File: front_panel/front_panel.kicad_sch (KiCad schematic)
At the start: 48 parts, among them J1 Conn_01x03_Socket, J10 Conn_01x02_Socket, J11 Conn_01x02_Socket, J12 Conn_01x02_Socket, J13 Conn_01x02_Socket, J14 Conn_01x02_Socket, J15 Conn_01x02_Socket, J16 Conn_01x02_Socket, J17 Conn_01x02_Socket, J18 Conn_01x02_Socket, J2 Conn_01x02_Socket, J20 Conn_01x02_Socket, J3 Conn_01x02_Socket, J4 Conn_01x04_Socket, J5 Conn_01x02_Socket, J5 Conn_01x03_Pin, J6 Conn_01x05_Pin, J7 Conn_01x02_Socket, J7 Conn_01x03_Pin, J8 Conn_01x02_Socket, J9 Conn_01x02_Socket, Q1 DMN3023L, Q2 DMN3023L, SW1 RotaryEncoder_Switch, SW2 SW_MEC_5G, SW3 SW_MEC_5G, U10 MCP9700x-ETT, U11 MCP33141D-05, U2 LM4040DBZ-4.1, U3 NCS21804, U4 CD74HC4067M, U5 DAC60501, U6 MIC5504-1.8YM5, U7 BP, U8 CD74HC4067M, U9 MCP9700x-ETT

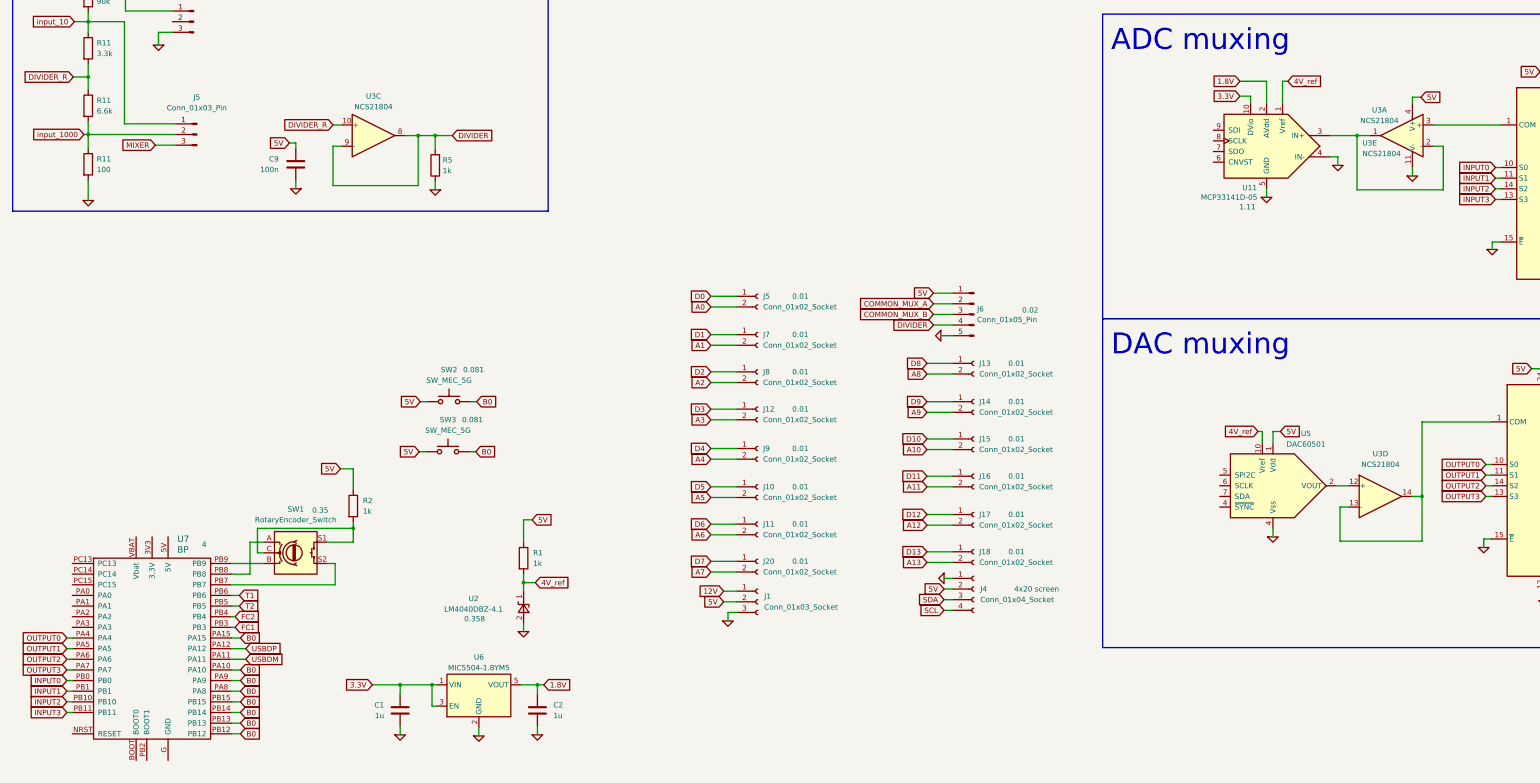
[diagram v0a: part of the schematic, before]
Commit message: Konačno PCB za BJT modul je počeo.
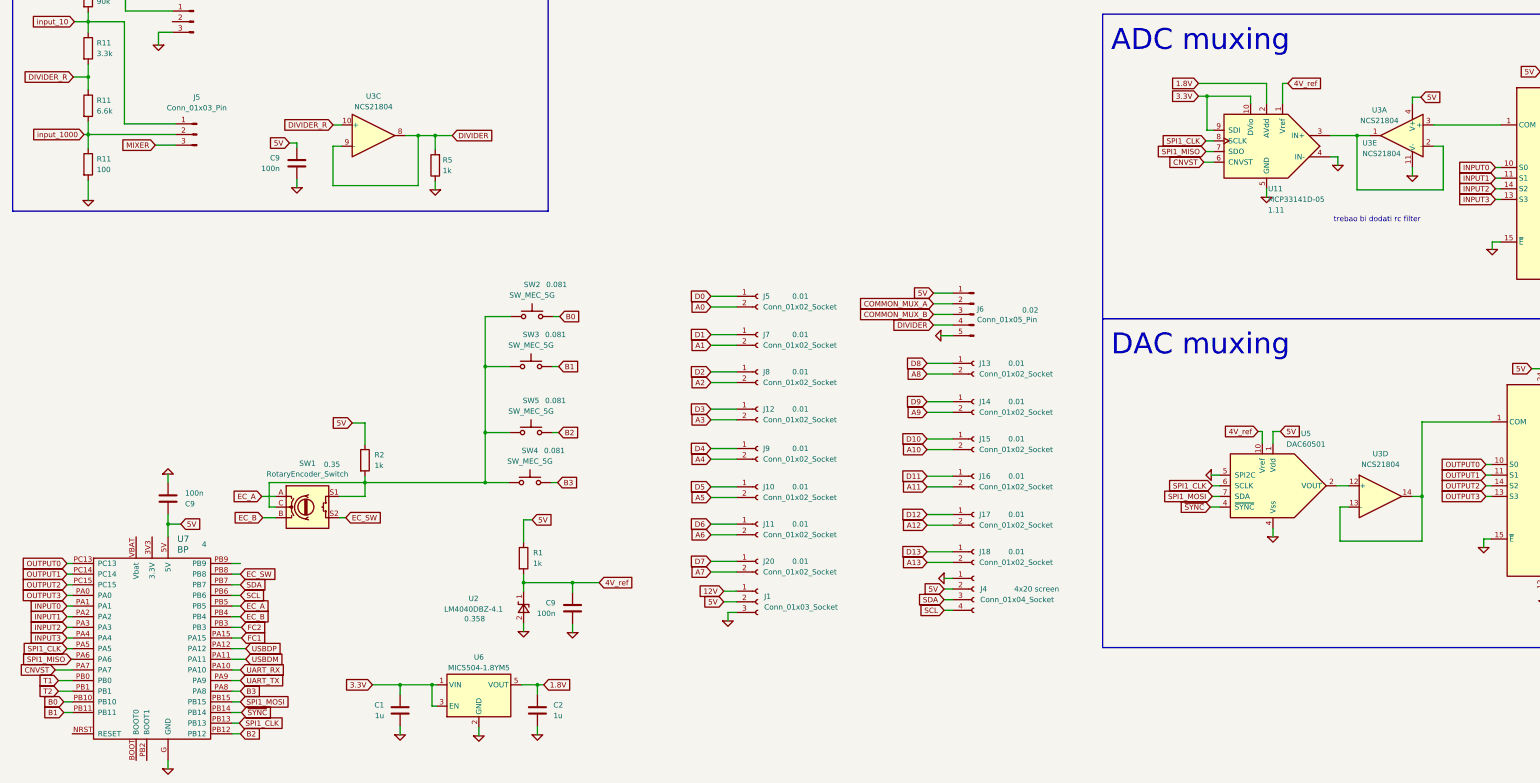
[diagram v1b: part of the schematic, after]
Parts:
- removed U11: MCP33141D-05, Package_SO:MSOP-10_3x3mm_P0.5mm, symbol SPICE_ADC:MCP33151D-05
- added C9 (x2): 100n, Capacitor_SMD:C_0603_1608Metric_Pad1.08x0.95mm_HandSolder, symbol Device:C
- added SW4, SW5: SW_MEC_5G, Button_Switch_SMD:SW_SPST_B3S-1000, symbol Switch:SW_MEC_5G
- added U11: MCP33141D-05, Package_SO:MSOP-10_3x3mm_P0.5mm, symbol SPICE_ADC:MCP33141D-05
- SW1: footprint (none) -> Rotary_Encoder:RotaryEncoder_Alps_EC12E-Switch_Vertical_H20mm
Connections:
- net 0: now also U5.5 (SPI2C), U7.G (GND), C9.2, C9.2, U11.4 (IN-), U11.5 (GND)
- net 1.8V: now also U11.2 (AVdd)
- net 3.3V: now also U11.10 (DVio), U11.9 (SDI)
- net 4V_ref: now also C9.1, U11.1 (Vref)
- net 5V: now also U7.5V, C9.1; no longer SW2.1 (A), SW2.2 (A), SW3.1 (A), SW3.2 (A)
- net B0: now also U7.PB10; no longer SW3.3 (B), SW3.4 (B), U7.PA10, U7.PA15, U7.PA8, U7.PA9, U7.PB12, U7.PB13, U7.PB14, U7.PB15
- net FC1: now also U7.PA15; no longer U7.PB3
- net FC2: now also U7.PB3; no longer U7.PB4
- net INPUT0: now also U7.PA1; no longer U7.PB0
- net INPUT1: now also U7.PA2; no longer U7.PB1
- net INPUT2: now also U7.PA3; no longer U7.PB10
- net INPUT3: now also U7.PA4; no longer U7.PB11
- net OUTPUT0: now also U7.PC13; no longer U7.PA4
- net OUTPUT1: now also U7.PC14; no longer U7.PA5
- net OUTPUT2: now also U7.PC15; no longer U7.PA6
- net OUTPUT3: now also U7.PA0; no longer U7.PA7
- net SCL: now also U7.PB6
- net SDA: now also U7.PB7
- net T1: now also U7.PB0; no longer U7.PB6
- net T2: now also U7.PB1; no longer U7.PB5
- net EC_A: now reaches SW1.A
- net EC_A: now also U7.PB5; no longer U7.PB8
- net at U7.PB9: no longer SW1.B
- net at R2.2, SW1.C, SW1.S1: now also SW2.1 (A), SW2.2 (A), SW3.1 (A), SW3.2 (A), SW4.1 (A), SW4.2 (A), SW5.1 (A), SW5.2 (A)
- net EC_SW: now reaches SW1.S2
- net EC_SW: now also U7.PB8; no longer U7.PB7
- net at U3.1, U3.2 (-): now also U11.3 (IN+)
- net ~{SYNC}: now reaches U5.4 (~{SYNC})
- net ~{SYNC}: now also U7.PB14
- net SPI1_CLK: now reaches U5.6 (SCLK)
- net SPI1_CLK: now also U7.PA5, U7.PB13, U11.8 (SCLK)
- net SPI1_MOSI: now reaches U5.7 (SDA)
- net SPI1_MOSI: now also U7.PB15
- new net B1: SW3.3 (B), SW3.4 (B), U7.PB11
- new net B2: SW5.3 (B), SW5.4 (B), U7.PB12
- new net B3: SW4.3 (B), SW4.4 (B), U7.PA8
- new net CNVST: U11.6 (CNVST), U7.PA7
- new net EC_B: SW1.B, U7.PB4
- new net SPI1_MISO: U11.7 (SDO), U7.PA6
- new net UART_RX: U7.PA10
- new net UART_TX: U7.PA9
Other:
- note added: "trebao bi dodati rc filter"
- moved on the sheet: R2, SW1, SW2, SW3
